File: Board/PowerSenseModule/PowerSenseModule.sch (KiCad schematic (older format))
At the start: 17 parts, among them J1 Power IO, J2 CAN IO, U1 TPS82150

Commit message: Added/Changed footprints
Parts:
- C8: footprint Capacitor_SMD:CP_Elec_6.3x5.8 -> Capacitor_SMD:CP_Elec_4x5.8
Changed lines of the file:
@@
 F 0 "C8" H 8315 1996 50  0000 L CNN
 F 1 "47uF" H 8315 1905 50  0000 L CNN
-F 2 "Capacitor_SMD:CP_Elec_6.3x5.8" H 8238 1800 50  0001 C CNN
+F 2 "Capacitor_SMD:CP_Elec_4x5.8" H 8238 1800 50  0001 C CNN
 F 3 "~" H 8200 1950 50  0001 C CNN
 	1    8200 1950

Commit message: Moses's changes, removed MPLAB proj
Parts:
- J1: footprint Connector_TE:DT13-4P -> Connector_TE:DT13-6P
- J2: footprint Connector_TE:DT13-2P -> Connector_TE:DT13-6P
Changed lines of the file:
@@
 F 0 "J2" H 1108 4681 50  0000 C CNN
 F 1 "CAN IO" H 1108 4590 50  0000 C CNN
-F 2 "Connector_TE:DT13-2P" H 1000 4500 50  0001 C CNN
+F 2 "Connector_TE:DT13-6P" H 1000 4500 50  0001 C CNN
 F 3 "~" H 1000 4500 50  0001 C CNN
 	1    1000 4500
@@
 F 0 "J1" H 1108 2981 50  0000 C CNN
 F 1 "Power IO" H 1108 2890 50  0000 C CNN
-F 2 "Connector_TE:DT13-4P" H 1000 2700 50  0001 C CNN
+F 2 "Connector_TE:DT13-6P" H 1000 2700 50  0001 C CNN
 F 3 "~" H 1000 2700 50  0001 C CNN
 	1    1000 2700

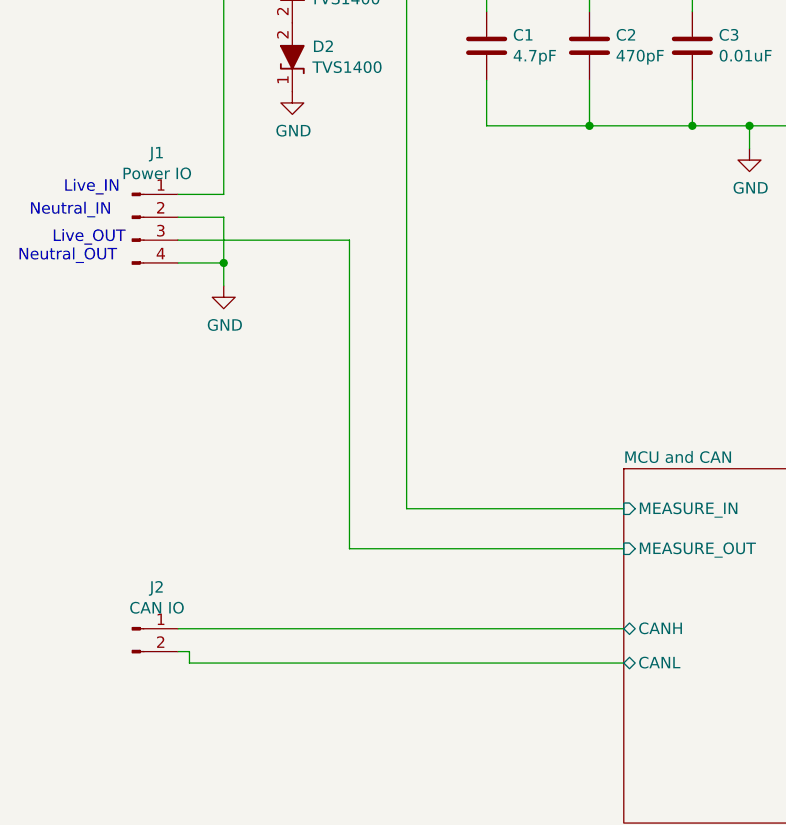
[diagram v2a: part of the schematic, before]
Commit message: Merged power and CAN connectors to one connector
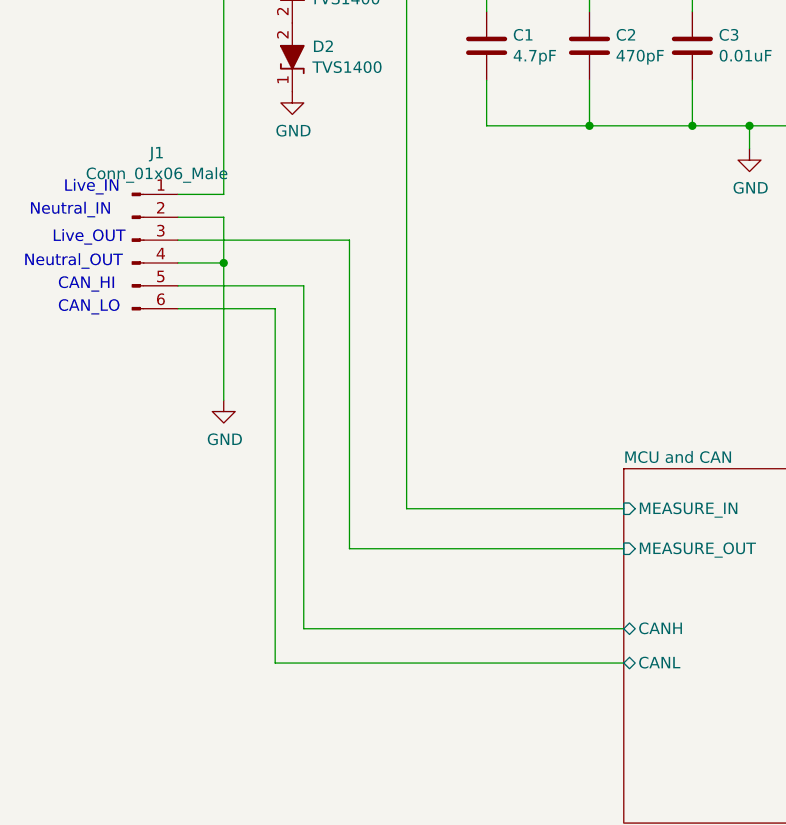
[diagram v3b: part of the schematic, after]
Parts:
- removed J1: Power IO, Connector_TE:DT13-6P, symbol Connector:Conn_01x04_Male
- removed J2: CAN IO, Connector_TE:DT13-6P, symbol Connector:Conn_01x02_Male
- added J1: Conn_01x06_Male, Connector_TE:DT13-6P, symbol Connector:Conn_01x06_Male
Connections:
- net +12V: now also J1.1 (Pin_1)
- net GND: now also J1.2 (Pin_2), J1.4 (Pin_4)
- net MCU and CAN/CANH: now also J1.5 (Pin_5)
- net MCU and CAN/CANL: now also J1.6 (Pin_6)
- net MCU and CAN/MEASURE_OUT: now also J1.3 (Pin_3)
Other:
- note added: "CAN_HI\n"
- note added: "CAN_LO"
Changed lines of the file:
@@
 Comment4 ""
 $EndDescr
-$Comp
-L Connector:Conn_01x02_Male J2
-U 1 1 5D28FA5A
-P 1000 4500
-F 0 "J2" H 1108 4681 50  0000 C CNN
-F 1 "CAN IO" H 1108 4590 50  0000 C CNN
-F 2 "Connector_TE:DT13-6P" H 1000 4500 50  0001 C CNN
-F 3 "~" H 1000 4500 50  0001 C CNN
-	1    1000 4500
-	1    0    0    -1
-$EndComp
-Wire Wire Line
-	1200 4600 1250 4600
-Wire Wire Line
-	1250 4600 1250 4650
 Wire Wire Line
 	1950 2800 1200 2800
@@
 	1200 2900 1400 2900
 Wire Wire Line
-	1400 2900 1400 3000
+	1400 2900 1400 3500
 $Comp
 L power:GND #PWR01
 U 1 1 5D342EEF
-P 1400 3000
-F 0 "#PWR01" H 1400 2750 50  0001 C CNN
-F 1 "GND" H 1405 2827 50  0000 C CNN
-F 2 "" H 1400 3000 50  0001 C CNN
-F 3 "" H 1400 3000 50  0001 C CNN
-	1    1400 3000
-	1    0    0    -1
-$EndComp
-Text Notes 500  2900 0    50   ~ 0
+P 1400 3500
+F 0 "#PWR01" H 1400 3250 50  0001 C CNN
+F 1 "GND" H 1405 3327 50  0000 C CNN
+F 2 "" H 1400 3500 50  0001 C CNN
+F 3 "" H 1400 3500 50  0001 C CNN
+	1    1400 3500
+	1    0    0    -1
+$EndComp
+Text Notes 525  2925 0    50   ~ 0
 Neutral_OUT
 Text Notes 650  2900 0    50   ~ 0
@@
 Text Notes 700  2600 0    50   ~ 0
 Live_IN\n
-$Comp
-L Connector:Conn_01x04_Male J1
-U 1 1 5D2865FC
-P 1000 2700
-F 0 "J1" H 1108 2981 50  0000 C CNN
-F 1 "Power IO" H 1108 2890 50  0000 C CNN
-F 2 "Connector_TE:DT13-6P" H 1000 2700 50  0001 C CNN
-F 3 "~" H 1000 2700 50  0001 C CNN
-	1    1000 2700
-	1    0    0    -1
-$EndComp
 $Comp
 L Device:Net-Tie_3_Tee NT1
@@
 	1    0    0    -1
 $EndComp
-Wire Wire Line
-	1250 4650 3150 4650
-Wire Wire Line
-	1200 4500 3150 4500
 $Sheet
 S 3150 3800 1700 1550
@@
 Wire Wire Line
 	1950 4150 1950 2800
+Wire Wire Line
+	3150 4500 1750 4500
+Wire Wire Line
+	1750 4500 1750 3000
+Wire Wire Line
+	1750 3000 1200 3000
+Wire Wire Line
+	3150 4650 1625 4650
+Wire Wire Line
+	1625 4650 1625 3100
+Wire Wire Line
+	1625 3100 1200 3100
+$Comp
+L Connector:Conn_01x06_Male J1
+U 1 1 5D4A20AB
+P 1000 2800
+F 0 "J1" H 1108 3181 50  0000 C CNN
+F 1 "Conn_01x06_Male" H 1108 3090 50  0000 C CNN
+F 2 "Connector_TE:DT13-6P" H 1000 2800 50  0001 C CNN
+F 3 "https://www.te.com/commerce/DocumentDelivery/DDEController?Action=showdoc&DocId=Customer+Drawing%7FDT13-4P%7FC%7Fpdf%7FEnglish%7FENG_CD_DT13-4P_C.pdf%7FDT13-4P" H 1000 2800 50  0001 C CNN
+	1    1000 2800
+	1    0    0    -1
+$EndComp
+Text Notes 675  3025 0    50   ~ 0
+CAN_HI\n
+Text Notes 675  3125 0    50   ~ 0
+CAN_LO
 $EndSCHEMATC

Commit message: Updated symbol fields and changed CAN transceiver package to make it easier to solder
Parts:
- U1: Manufacturer (none) -> TI; Manufacturer PN (none) -> TPS82150SILR; Price 1 QTY (none) -> 3.03; Supplier (none) -> Mouser; Supplier Link (none) -> https://www.mouser.com/ProductDetail/?qs=gt1LBUVyoHksxpRVOm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; Supplier PN (none) -> 595-TPS82150SILR

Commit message: Added charge pump
Added charge pump for OP amp positive supply rail and reorganized the MCU page.
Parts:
- removed D1, D2: TVS1400, Package_SON_Custom:WSON-6-2NET-1EP_2x2mm_P0.65mm_EP1x1.6mm, symbol F1_TVS_Diodes:TVS1400
- added C? (x4): 0.1uF, symbol Device:C
- added C?: 4.7uF, symbol Device:CP
- added D?: SD05-7, Diode_SMD:D_SOD-323_HandSoldering, symbol Device:D_Zener
- added D? (x4): D, symbol Device:D
- C6, C8: symbol Device:C -> Device:CP
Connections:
- net +12V: now also D?.1 (K), D?.2 (A)
- net GND: now also D?.2 (A)
- net GNDA: now also C?.2, C?.2, C?.2
- new net: C?.1, D?.1 (K), D?.2 (A) (x3)
- new net PWM: C?.2, C?.2
- new net VS: C?.1, C?.1, D?.1 (K)
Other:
- note added: "Unloaded +22V out\n"

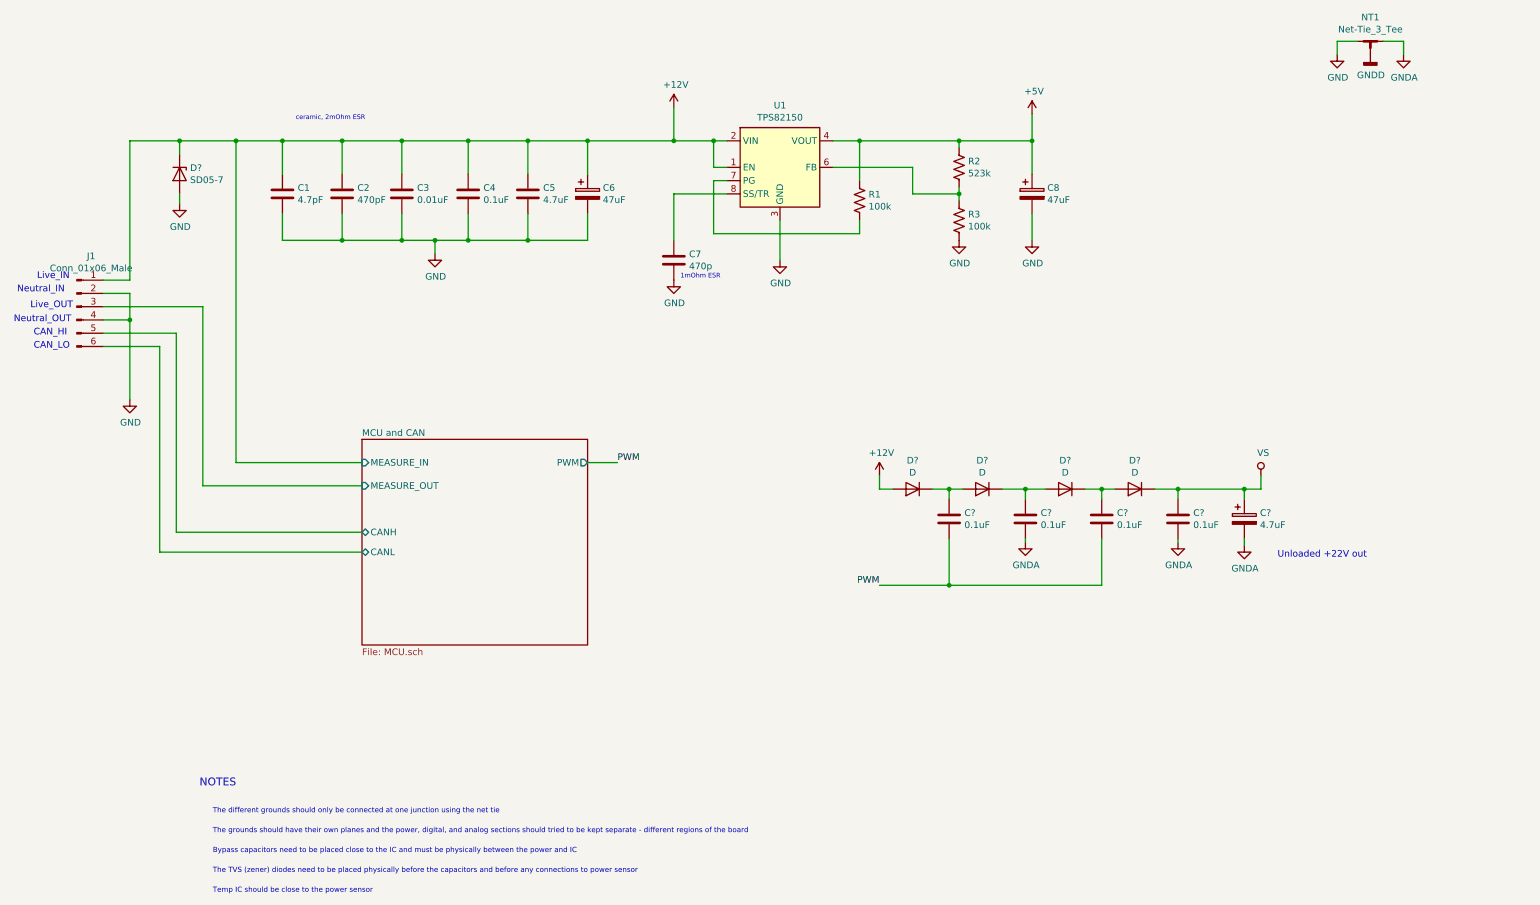
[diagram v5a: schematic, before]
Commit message: Annotated new symbols
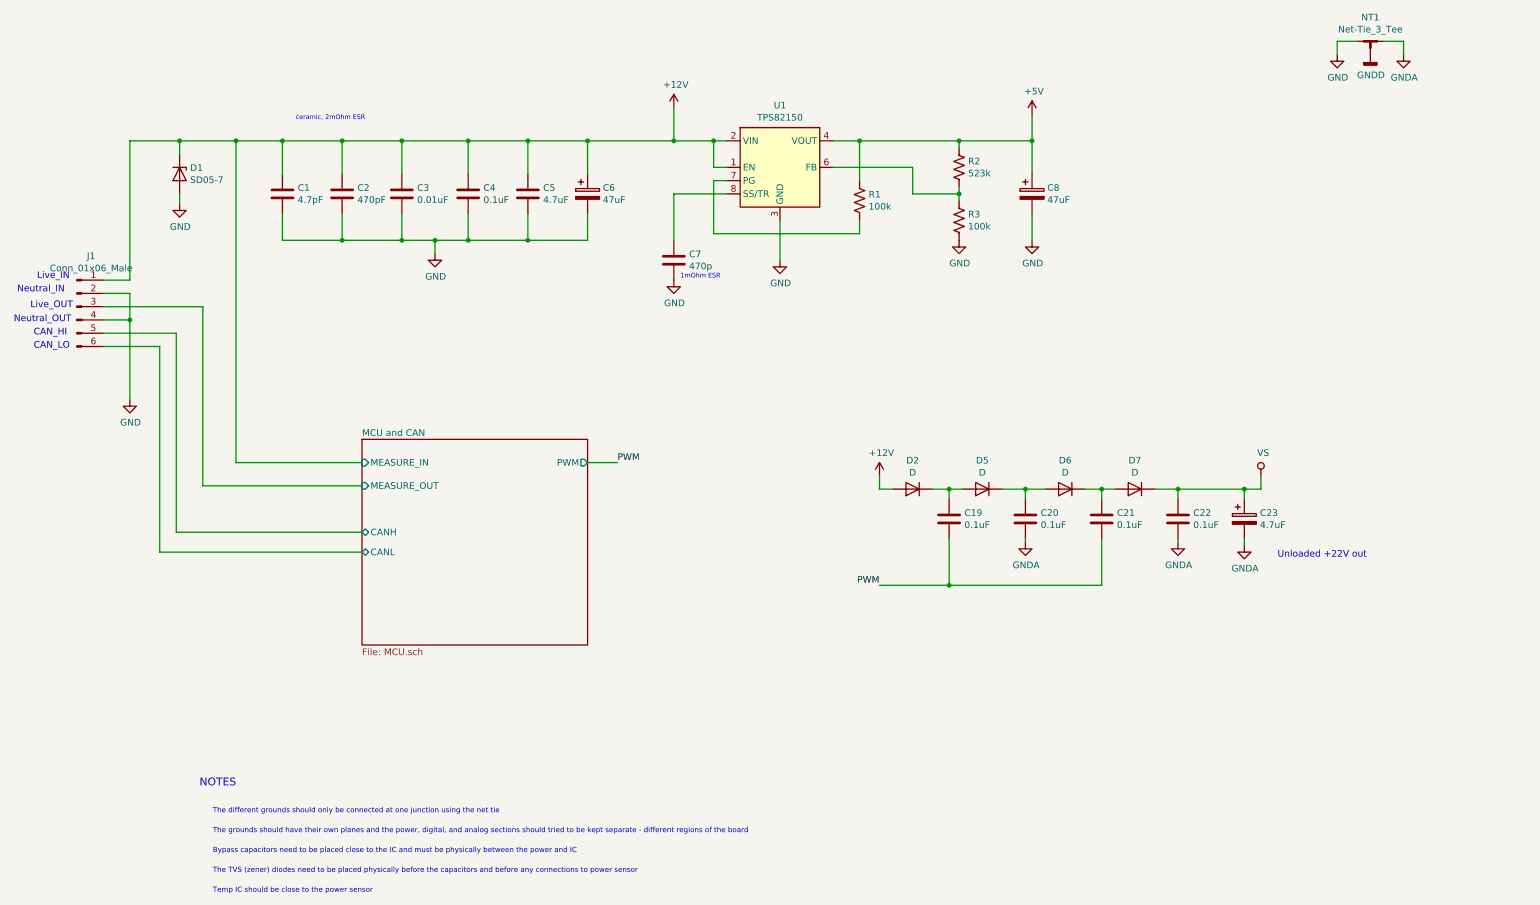
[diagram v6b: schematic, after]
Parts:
- gave numbers to parts that had none: 10
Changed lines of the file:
@@
 	1400 1550 1775 1550
 $Comp
-L Device:D_Zener D?
+L Device:D_Zener D1
 U 1 1 5DEFEB23
 P 1775 1800
-F 0 "D?" V 1729 1879 50  0000 L CNN
+F 0 "D1" V 1729 1879 50  0000 L CNN
 F 1 "SD05-7" V 1820 1879 50  0000 L CNN
 F 2 "Diode_SMD:D_SOD-323_HandSoldering" H 1775 1800 50  0001 C CNN
@@
 	1775 1550 2200 1550
 $Comp
-L power:GND #PWR?
+L power:GND #PWR02
 U 1 1 5DF00A75
 P 1775 2025
-F 0 "#PWR?" H 1775 1775 50  0001 C CNN
+F 0 "#PWR02" H 1775 1775 50  0001 C CNN
 F 1 "GND" H 1780 1852 50  0000 C CNN
 F 2 "" H 1775 2025 50  0001 C CNN
@@
 	1775 2025 1775 1950
 $Comp
-L Device:D D?
+L Device:D D2
 U 1 1 5E37B877
 P 7300 4175
-F 0 "D?" H 7300 3959 50  0000 C CNN
+F 0 "D2" H 7300 3959 50  0000 C CNN
 F 1 "D" H 7300 4050 50  0000 C CNN
 F 2 "" H 7300 4175 50  0001 C CNN
@@
 $EndComp
 $Comp
-L Device:D D?
+L Device:D D5
 U 1 1 5E37C9F3
 P 7825 4175
-F 0 "D?" H 7825 3959 50  0000 C CNN
+F 0 "D5" H 7825 3959 50  0000 C CNN
 F 1 "D" H 7825 4050 50  0000 C CNN
 F 2 "" H 7825 4175 50  0001 C CNN
@@
 $EndComp
 $Comp
-L Device:C C?
+L Device:C C20
 U 1 1 5E37E7E2
 P 8150 4400
-F 0 "C?" H 8265 4446 50  0000 L CNN
+F 0 "C20" H 8265 4446 50  0000 L CNN
 F 1 "0.1uF" H 8265 4355 50  0000 L CNN
 F 2 "" H 8188 4250 50  0001 C CNN
@@
 $EndComp
 $Comp
-L Device:C C?
+L Device:C C19
 U 1 1 5E37E843
 P 7575 4400
-F 0 "C?" H 7690 4446 50  0000 L CNN
+F 0 "C19" H 7690 4446 50  0000 L CNN
 F 1 "0.1uF" H 7690 4355 50  0000 L CNN
 F 2 "" H 7613 4250 50  0001 C CNN
@@
 	7050 4175 7050 4075
 $Comp
-L power:+12V #PWR?
+L power:+12V #PWR010
 U 1 1 5E389ACF
 P 7050 4075
-F 0 "#PWR?" H 7050 3925 50  0001 C CNN
+F 0 "#PWR010" H 7050 3925 50  0001 C CNN
 F 1 "+12V" H 7065 4248 50  0000 C CNN
 F 2 "" H 7050 4075 50  0001 C CNN
@@
 	7575 4550 7575 4900
 $Comp
-L power:GNDA #PWR?
+L power:GNDA #PWR022
 U 1 1 5E38CDB2
 P 8150 4575
-F 0 "#PWR?" H 8150 4325 50  0001 C CNN
+F 0 "#PWR022" H 8150 4325 50  0001 C CNN
 F 1 "GNDA" H 8155 4402 50  0000 C CNN
 F 2 "" H 8150 4575 50  0001 C CNN
@@
 	8150 4575 8150 4550
 $Comp
-L Device:D D?
+L Device:D D6
 U 1 1 5E394EB5
 P 8450 4175
-F 0 "D?" H 8450 3959 50  0000 C CNN
+F 0 "D6" H 8450 3959 50  0000 C CNN
 F 1 "D" H 8450 4050 50  0000 C CNN
 F 2 "" H 8450 4175 50  0001 C CNN
@@
 $EndComp
 $Comp
-L Device:D D?
+L Device:D D7
 U 1 1 5E394EBB
 P 8975 4175
-F 0 "D?" H 8975 3959 50  0000 C CNN
+F 0 "D7" H 8975 3959 50  0000 C CNN
 F 1 "D" H 8975 4050 50  0000 C CNN
 F 2 "" H 8975 4175 50  0001 C CNN
@@
 $EndComp
 $Comp
-L Device:C C?
+L Device:C C22
 U 1 1 5E394EC1
 P 9300 4400
-F 0 "C?" H 9415 4446 50  0000 L CNN
+F 0 "C22" H 9415 4446 50  0000 L CNN
 F 1 "0.1uF" H 9415 4355 50  0000 L CNN
 F 2 "" H 9338 4250 50  0001 C CNN
@@
 $EndComp
 $Comp
-L Device:C C?
+L Device:C C21
 U 1 1 5E394EC7
 P 8725 4400
-F 0 "C?" H 8840 4446 50  0000 L CNN
+F 0 "C21" H 8840 4446 50  0000 L CNN
 F 1 "0.1uF" H 8840 4355 50  0000 L CNN
 F 2 "" H 8763 4250 50  0001 C CNN
@@
 	9300 4175 9125 4175
 $Comp
-L power:GNDA #PWR?
+L power:GNDA #PWR027
 U 1 1 5E394ED5
 P 9300 4575
-F 0 "#PWR?" H 9300 4325 50  0001 C CNN
+F 0 "#PWR027" H 9300 4325 50  0001 C CNN
 F 1 "GNDA" H 9305 4402 50  0000 C CNN
 F 2 "" H 9300 4575 50  0001 C CNN
@@
 Connection ~ 9300 4175
 $Comp
-L power:VS #PWR?
+L power:VS #PWR034
 U 1 1 5E3A54BD
 P 9925 4075
-F 0 "#PWR?" H 9725 3925 50  0001 C CNN
+F 0 "#PWR034" H 9725 3925 50  0001 C CNN
 F 1 "VS" H 9942 4248 50  0000 C CNN
 F 2 "" H 9925 4075 50  0001 C CNN
@@
 	2200 1550 2550 1550
 $Comp
-L Device:CP C?
+L Device:CP C23
 U 1 1 5E3BD7DC
 P 9800 4400
-F 0 "C?" H 9918 4446 50  0000 L CNN
+F 0 "C23" H 9918 4446 50  0000 L CNN
 F 1 "4.7uF" H 9918 4355 50  0000 L CNN
 F 2 "" H 9838 4250 50  0001 C CNN
@@
 	9800 4175 9925 4175
 $Comp
-L power:GNDA #PWR?
+L power:GNDA #PWR029
 U 1 1 5E3C0B37
 P 9800 4600
-F 0 "#PWR?" H 9800 4350 50  0001 C CNN
+F 0 "#PWR029" H 9800 4350 50  0001 C CNN
 F 1 "GNDA" H 9805 4427 50  0000 C CNN
 F 2 "" H 9800 4600 50  0001 C CNN

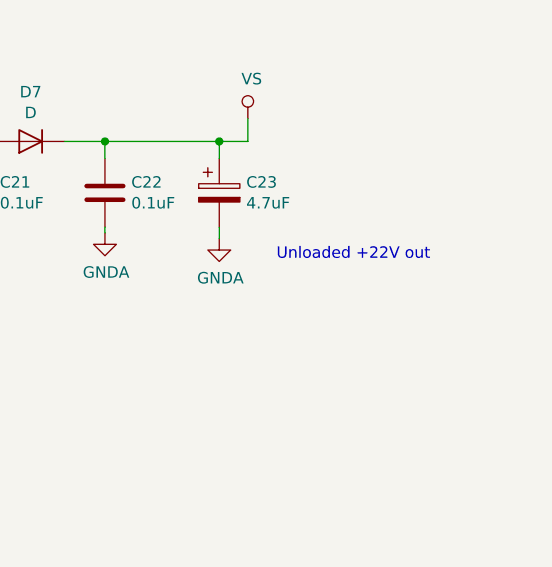
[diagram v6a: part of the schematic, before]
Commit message: Added diode footprints to charge pump and changed oscillator caps from 10u to 10p
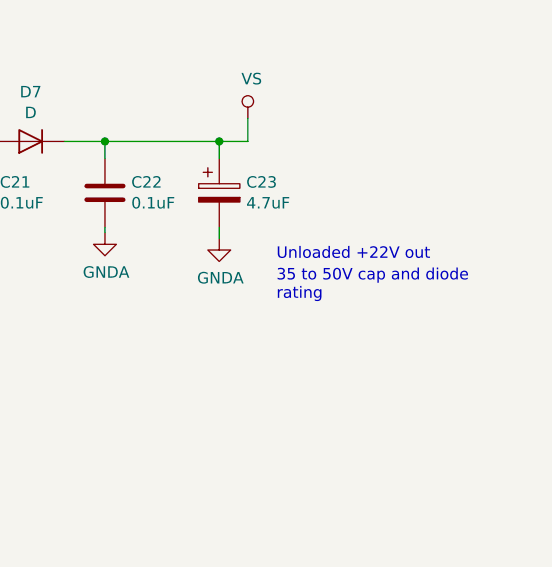
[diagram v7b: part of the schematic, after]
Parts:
- C19, C20, C21, C22: footprint (none) -> Capacitor_SMD:C_0603_1608Metric
- C23: footprint (none) -> Capacitor_SMD:CP_Elec_4x5.8
- D2, D5, D6, D7: footprint (none) -> Diode_SMD:D_SOD-323_HandSoldering; Supplier Link (none) -> https://www.mouser.com/ProductDetail/Toshiba/CUS10S30H3F?qs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
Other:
- note added: "35 to 50V cap and diode \nrating\n"
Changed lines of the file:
@@
 F 0 "D2" H 7300 3959 50  0000 C CNN
 F 1 "D" H 7300 4050 50  0000 C CNN
-F 2 "" H 7300 4175 50  0001 C CNN
-F 3 "~" H 7300 4175 50  0001 C CNN
+F 2 "Diode_SMD:D_SOD-323_HandSoldering" H 7300 4175 50  0001 C CNN
+F 3 "http://toshiba.semicon-storage.com/ap-en/product/diode/sbd/detail.CUS10S30.html" H 7300 4175 50  0001 C CNN
+F 4 "https://www.mouser.com/ProductDetail/Toshiba/CUS10S30H3F?qs=sGAEpiMZZMtQ8nqTKtFS%2FLnbHK8U7YHpoD%2FnZkbvIUu50yFANYtBSg%3D%3D" H 7300 4175 50  0001 C CNN "Supplier Link"
 	1    7300 4175
 	-1   0    0    1
@@
 F 0 "D5" H 7825 3959 50  0000 C CNN
 F 1 "D" H 7825 4050 50  0000 C CNN
-F 2 "" H 7825 4175 50  0001 C CNN
-F 3 "~" H 7825 4175 50  0001 C CNN
+F 2 "Diode_SMD:D_SOD-323_HandSoldering" H 7825 4175 50  0001 C CNN
+F 3 "http://toshiba.semicon-storage.com/ap-en/product/diode/sbd/detail.CUS10S30.html" H 7825 4175 50  0001 C CNN
+F 4 "https://www.mouser.com/ProductDetail/Toshiba/CUS10S30H3F?qs=sGAEpiMZZMtQ8nqTKtFS%2FLnbHK8U7YHpoD%2FnZkbvIUu50yFANYtBSg%3D%3D" H 7825 4175 50  0001 C CNN "Supplier Link"
 	1    7825 4175
 	-1   0    0    1
@@
 F 0 "C20" H 8265 4446 50  0000 L CNN
 F 1 "0.1uF" H 8265 4355 50  0000 L CNN
-F 2 "" H 8188 4250 50  0001 C CNN
+F 2 "Capacitor_SMD:C_0603_1608Metric" H 8188 4250 50  0001 C CNN
 F 3 "~" H 8150 4400 50  0001 C CNN
 	1    8150 4400
@@
 F 0 "C19" H 7690 4446 50  0000 L CNN
 F 1 "0.1uF" H 7690 4355 50  0000 L CNN
-F 2 "" H 7613 4250 50  0001 C CNN
+F 2 "Capacitor_SMD:C_0603_1608Metric" H 7613 4250 50  0001 C CNN
 F 3 "~" H 7575 4400 50  0001 C CNN
 	1    7575 4400
@@
 F 0 "D6" H 8450 3959 50  0000 C CNN
 F 1 "D" H 8450 4050 50  0000 C CNN
-F 2 "" H 8450 4175 50  0001 C CNN
-F 3 "~" H 8450 4175 50  0001 C CNN
+F 2 "Diode_SMD:D_SOD-323_HandSoldering" H 8450 4175 50  0001 C CNN
+F 3 "http://toshiba.semicon-storage.com/ap-en/product/diode/sbd/detail.CUS10S30.html" H 8450 4175 50  0001 C CNN
+F 4 "https://www.mouser.com/ProductDetail/Toshiba/CUS10S30H3F?qs=sGAEpiMZZMtQ8nqTKtFS%2FLnbHK8U7YHpoD%2FnZkbvIUu50yFANYtBSg%3D%3D" H 8450 4175 50  0001 C CNN "Supplier Link"
 	1    8450 4175
 	-1   0    0    1
@@
 F 0 "D7" H 8975 3959 50  0000 C CNN
 F 1 "D" H 8975 4050 50  0000 C CNN
-F 2 "" H 8975 4175 50  0001 C CNN
-F 3 "~" H 8975 4175 50  0001 C CNN
+F 2 "Diode_SMD:D_SOD-323_HandSoldering" H 8975 4175 50  0001 C CNN
+F 3 "http://toshiba.semicon-storage.com/ap-en/product/diode/sbd/detail.CUS10S30.html" H 8975 4175 50  0001 C CNN
+F 4 "https://www.mouser.com/ProductDetail/Toshiba/CUS10S30H3F?qs=sGAEpiMZZMtQ8nqTKtFS%2FLnbHK8U7YHpoD%2FnZkbvIUu50yFANYtBSg%3D%3D" H 8975 4175 50  0001 C CNN "Supplier Link"
 	1    8975 4175
 	-1   0    0    1
@@
 F 0 "C22" H 9415 4446 50  0000 L CNN
 F 1 "0.1uF" H 9415 4355 50  0000 L CNN
-F 2 "" H 9338 4250 50  0001 C CNN
+F 2 "Capacitor_SMD:C_0603_1608Metric" H 9338 4250 50  0001 C CNN
 F 3 "~" H 9300 4400 50  0001 C CNN
 	1    9300 4400
@@
 F 0 "C21" H 8840 4446 50  0000 L CNN
 F 1 "0.1uF" H 8840 4355 50  0000 L CNN
-F 2 "" H 8763 4250 50  0001 C CNN
+F 2 "Capacitor_SMD:C_0603_1608Metric" H 8763 4250 50  0001 C CNN
 F 3 "~" H 8725 4400 50  0001 C CNN
 	1    8725 4400
@@
 F 0 "C23" H 9918 4446 50  0000 L CNN
 F 1 "4.7uF" H 9918 4355 50  0000 L CNN
-F 2 "" H 9838 4250 50  0001 C CNN
+F 2 "Capacitor_SMD:CP_Elec_4x5.8" H 9838 4250 50  0001 C CNN
 F 3 "~" H 9800 4400 50  0001 C CNN
 	1    9800 4400
@@
 Wire Wire Line
 	5075 3975 4850 3975
+Text Notes 10050 4875 0    50   ~ 0
+35 to 50V cap and diode \nrating\n
 $EndSCHEMATC
